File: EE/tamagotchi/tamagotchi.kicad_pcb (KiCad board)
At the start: 2 copper layers, 6.2 x 1.8 mm, 42 parts, among them J7 TAG_CONNECT, P1 USB_C_Plug_USB2.0, SW2 TL1260BQRBLK, U2 STM32G031G8Ux

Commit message: Basic Placement Complete
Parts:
- removed D2: LED, LED_SMD:LED_0603_1608Metric_Pad1.05x0.95mm_HandSolder
- removed R1: R, Resistor_SMD:R_0402_1005Metric_Pad0.72x0.64mm_HandSolder
- added BATTERY: Conn_01x02_Male, Connector_JST:JST_PH_B2B-PH-K_1x02_P2.00mm_Vertical, F.Cu at (167.5, 107.3)
- added D3: LED_BRGY, Library:EAST1616RGYA0_EVE, F.Cu at (169.2, 87.2)
- added D4: LED_BRGY, Library:EAST1616RGYA0_EVE, F.Cu at (152.7, 72.6)
- added D5: LED_BRGY, Library:EAST1616RGYA0_EVE, F.Cu at (137.5, 87.2)
- added J3: Conn_01x07, Library:MOLEX_532610771, B.Cu at (152.0, 79.5)
- added JP2: SolderJumper_2_Bridged, Jumper:SolderJumper-2_P1.3mm_Bridged2Bar_RoundedPad1.0x1.5mm, F.Cu at (165.5, 100.9)
- added JP3: SolderJumper_2_Bridged, Jumper:SolderJumper-2_P1.3mm_Bridged2Bar_RoundedPad1.0x1.5mm, F.Cu at (156.0, 100.1)
- added JP4: SolderJumper_2_Bridged, Jumper:SolderJumper-2_P1.3mm_Bridged2Bar_RoundedPad1.0x1.5mm, B.Cu at (160.8, 102.5)
- added L1: ~, Library:UT Transformer, F.Cu at (161.5, 105.8)
- added Q1: Q_NMOS_GSD, Package_TO_SOT_SMD:SOT-23, B.Cu at (155.5, 87.9)
- added Q2: Q_NMOS_GSD, Package_TO_SOT_SMD:SOT-23, F.Cu at (166.2, 78.8)
- added Q3: Q_NMOS_GSD, Package_TO_SOT_SMD:SOT-23, F.Cu at (141.9, 78.2)
- added Q4: Q_NMOS_GSD, Package_TO_SOT_SMD:SOT-23, F.Cu at (161.8, 98.0)
- added Q5: Q_PMOS_GSD, Package_TO_SOT_SMD:SOT-23, F.Cu at (162.4, 91.8)
- added Q7: Q_NMOS_GSD, Package_TO_SOT_SMD:SOT-23, F.Cu at (165.7, 84.3)
- added UT: Conn_01x02_Male, Connector_JST:JST_PH_B2B-PH-K_1x02_P2.00mm_Vertical, F.Cu at (157.0, 107.2)
- C1, D1, D6, D7, D8, D9, J7, R14, R15, R16, R17, R2, R27, R28, R3, R4: moved to B.Cu
- moved R29 81.1 mm to (141.2, 86.3), turned to 90 degrees
- moved C5 78.6 mm to (151.8, 92.2), turned to -90 degrees
- moved R28 78.3 mm to (164.2, 76.4), turned to -90 degrees
- moved R27 75.8 mm to (165.8, 76.4), turned to -90 degrees
- moved R13 75.5 mm to (137.2, 90.1), turned to 90 degrees
- moved R10 73.7 mm to (149.9, 72.0)
- moved J7 54.9 mm to (144.5, 96.5)
- moved R9 53.5 mm to (163.0, 77.8), turned to 0 degrees
- moved R8 51.0 mm to (162.4, 79.4), turned to -90 degrees
- moved R7 49.5 mm to (169.8, 84.2), turned to -90 degrees
- moved R12 46.1 mm to (138.8, 77.2)
- moved R11 43.8 mm to (138.2, 79.1), turned to -90 degrees
- moved C1 43.6 mm to (147.2, 84.5), turned to -90 degrees
- moved R5 42.4 mm to (161.9, 84.6), turned to -90 degrees
- moved R4 42.0 mm to (158.7, 86.9)
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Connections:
- JP1 pad 1: /Power/VBAT_BRIDGED -> Net-(J8-Pin_1)
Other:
- board size 6.2 x 1.8 mm -> 34.8 x 38.8 mm

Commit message: Migrated to 4 Layer. Added 3v3 and gnd layers
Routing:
- added copper zone on In2.Cu, net +3V3
- added copper zone on In1.Cu, net GND
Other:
- copper layers 2 -> 4
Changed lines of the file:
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@@
 	(layers
 		(0 "F.Cu" signal)
+		(4 "In1.Cu" signal)
+		(6 "In2.Cu" signal)
 		(2 "B.Cu" signal)
 		(9 "F.Adhes" user "F.Adhesive")
@@
 	)
 	(setup
+		(stackup
+			(layer "F.SilkS"
+				(type "Top Silk Screen")
+			)
+			(layer "F.Paste"
+				(type "Top Solder Paste")
+			)
+			(layer "F.Mask"
+				(type "Top Solder Mask")
+				(thickness 0.01)
+			)
+			(layer "F.Cu"
+				(type "copper")
+				(thickness 0.035)
+			)
+			(layer "dielectric 1"
+				(type "prepreg")
+				(thickness 0.1)
+				(material "FR4")
+				(epsilon_r 4.5)
+				(loss_tangent 0.02)
+			)
+			(layer "In1.Cu"
+				(type "copper")
+				(thickness 0.035)
+			)
+			(layer "dielectric 2"
+				(type "core")
+				(thickness 1.24)
+				(material "FR4")
+				(epsilon_r 4.5)
+				(loss_tangent 0.02)
+			)
+			(layer "In2.Cu"
+				(type "copper")
+				(thickness 0.035)
+			)
+			(layer "dielectric 3"
+				(type "prepreg")
+				(thickness 0.1)
+				(material "FR4")
+				(epsilon_r 4.5)
+				(loss_tangent 0.02)
+			)
+			(layer "B.Cu"
+				(type "copper")
+				(thickness 0.035)
+			)
+			(layer "B.Mask"
+				(type "Bottom Solder Mask")
+				(thickness 0.01)
+			)
+			(layer "B.Paste"
+				(type "Bottom Solder Paste")
+			)
+			(layer "B.SilkS"
+				(type "Bottom Silk Screen")
+			)
+			(copper_finish "None")
+			(dielectric_constraints no)
+		)
 		(pad_to_mask_clearance 0)
 		(allow_soldermask_bridges_in_footprints no)
@@
 		(layer "Edge.Cuts")
 	)
+	(zone
+		(net 2)
+		(net_name "GND")
+		(layer "In1.Cu")
+		(hatch edge 0.5)
+		(connect_pads
+			(clearance 0.5)
+		)
+		(min_thickness 0.25)
+		(filled_areas_thickness no)
+		(fill yes
+			(thermal_gap 0.5)
+			(thermal_bridge_width 0.5)
+		)
+		(polygon
+			(pts
+				(xy 136 71) (xy 170.75 71) (xy 170.75 109.75) (xy 136 109.75)
+			)
+		)
+	)
+	(zone
+		(net 1)
+		(net_name "+3V3")
+		(layer "In2.Cu")
+		(hatch edge 0.5)
+		(priority 1)
+		(connect_pads
+			(clearance 0.5)
+		)
+		(min_thickness 0.25)
+		(filled_areas_thickness no)
+		(fill yes
+			(thermal_gap 0.5)
+			(thermal_bridge_width 0.5)
+		)
+		(polygon
+			(pts
+				(xy 136 71) (xy 170.75 71) (xy 170.75 109.75) (xy 136 109.75)
+			)
+		)
+	)
 	(embedded_fonts no)

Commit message: Minor Placement update
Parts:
- JP1, Q1, R3, R4: moved to F.Cu
- JP3: moved to B.Cu
- moved Q2 21.0 mm to (145.3, 76.8), turned to 90 degrees
- moved D1 19.7 mm to (153.4, 91.8)
- moved R2 19.7 mm to (156.2, 91.8)
- moved R9 18.9 mm to (144.3, 80.0), turned to 90 degrees
- moved Q7 18.2 mm to (151.8, 96.0), turned to -90 degrees
- moved R8 16.5 mm to (146.0, 80.6), turned to 0 degrees
- moved R6 13.5 mm to (153.0, 92.7), turned to -90 degrees
- moved D7 13.2 mm to (153.4, 72.2)
- moved R15 13.1 mm to (156.2, 72.2)
- moved R5 13.0 mm to (151.4, 92.2), turned to 180 degrees
- moved R11 12.8 mm to (150.9, 80.6), turned to 0 degrees
- moved Q1 11.1 mm to (155.2, 76.8), turned to 90 degrees
- moved R12 10.7 mm to (149.1, 80.0), turned to 90 degrees
- moved UT 10.4 mm to (167.4, 107.2)
- moved BATTERY 9.41 mm to (158.3, 105.2), turned to -90 degrees
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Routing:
- net VBUS: track 0.00 -> 13.3 mm

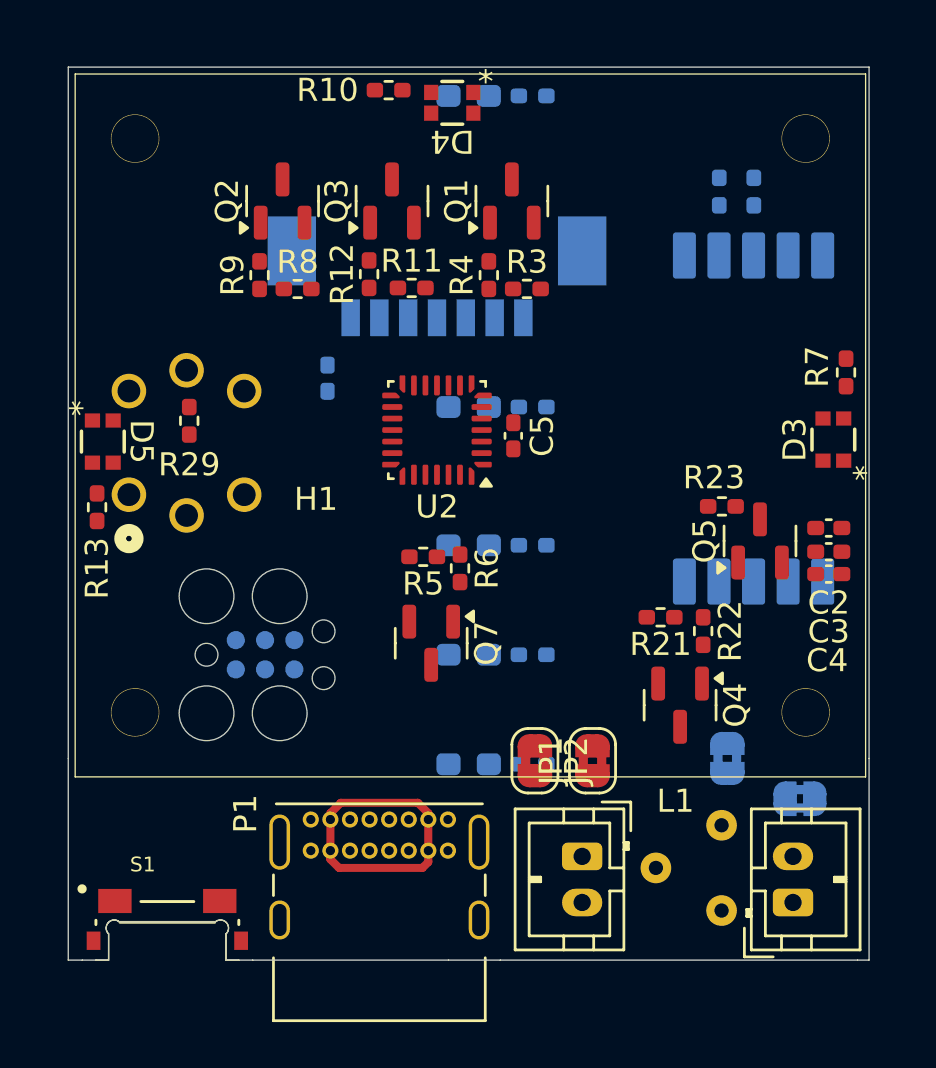
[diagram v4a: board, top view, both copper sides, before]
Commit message: Removed LEDs
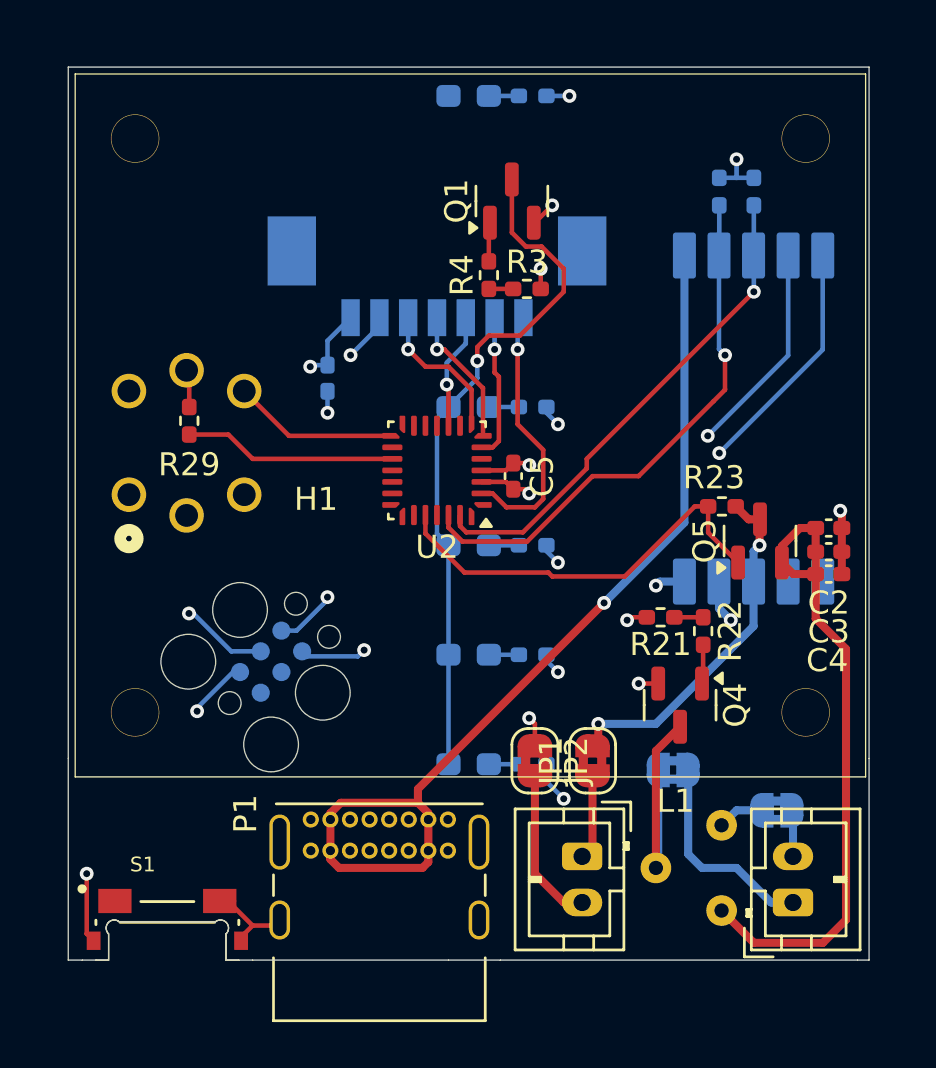
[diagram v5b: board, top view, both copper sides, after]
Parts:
- removed D3, D4, D5: LED_BRGY, Library:EAST1616RGYA0_EVE
- removed Q2, Q3, Q7: Q_NMOS_GSD, Package_TO_SOT_SMD:SOT-23
- removed R10, R13, R7: R, Resistor_SMD:R_0402_1005Metric_Pad0.72x0.64mm_HandSolder
- removed R11, R5, R8: 100k, Resistor_SMD:R_0402_1005Metric_Pad0.72x0.64mm_HandSolder
- removed R12, R6, R9: 33, Resistor_SMD:R_0402_1005Metric_Pad0.72x0.64mm_HandSolder
- moved JP3 2.40 mm to (162.2, 101.5), turned to 180 degrees
- moved C5 1.75 mm to (155.3, 88.8)
- moved U2 1.75 mm to (152.0, 88.5)
- moved JP4 1.12 mm to (166.8, 103.2)
- moved J7 0.40 mm to (144.8, 96.8), turned to 45 degrees
- renumbered UT to J1, BATTERY to J8
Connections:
- J3 pad 3: /Display/MOSI{SPI} -> /Display/MOSI
- J3 pad 4: /Display/CLK{SPI} -> /Display/CLK
- J3 pad 5: /Display/CS{SPI} -> /Display/CS
- J3 pad 6: /Display/DC{SPI} -> /Display/DC
- J3 pad 7: /Display/RST{SPI} -> /Display/RST
- J7 pad 5: /MCU/SWDCLK -> /MCU/SWCLK
- R29 pad 1: /Vape/VAPE_LED -> /MCU/VAPE_LED
- U2 pad 10: /MCU/CS{SPI} -> /Display/CS
- U2 pad 11: /MCU/DC{SPI} -> unconnected-(U2-PA5-Pad11)
- U2 pad 12: /MCU/RST{SPI} -> unconnected-(U2-PA6-Pad12)
- U2 pad 14: /Display/GREEN_EN -> unconnected-(U2-PB0-Pad14)
- U2 pad 15: /Display/YELLOW_EN -> /MCU/VAPE_SW
- U2 pad 17: unconnected-(U2-PC6-Pad17) -> /MCU/VAPE_LED
- U2 pad 2: unconnected-(U2-PC15-Pad2) -> /Display/RST
- U2 pad 22: /MCU/VAPE_SW -> unconnected-(U2-PA15-Pad22)
- U2 pad 23: /Display/RED_EN -> unconnected-(U2-PB3-Pad23)
- U2 pad 6: unconnected-(U2-PA0-Pad6) -> /Display/DC
- U2 pad 7: /MCU/CLK{SPI} -> /Display/CLK
- U2 pad 8: /MCU/MOSI{SPI} -> /Display/MOSI
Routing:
- net Net-(D1-K): track 0.00 -> 30.0 mm, vias 0 -> 1
- net VBUS: track 13.3 -> 41.8 mm, vias 0 -> 1
- net /Vape/VBAT_CONT: track 0.00 -> 28.1 mm
- net GND: track 0.00 -> 25.9 mm, vias 0 -> 12
- net /MCU/SCL: track 0.00 -> 23.6 mm, vias 0 -> 1
- net /MCU/SDA: track 0.00 -> 21.7 mm, vias 0 -> 1
- net /MCU/VAPE_EN_N: track 0.00 -> 18.1 mm
- net +3V3: track 0.00 -> 18.0 mm, vias 0 -> 10
- net /VBAT: track 0.00 -> 15.6 mm, vias 0 -> 2
- net /Display/RST: track 0.00 -> 11.5 mm, vias 0 -> 1
- net /Vape/UT_OUT-: track 0.00 -> 10.9 mm
- net /MCU/CE_N: track 0.00 -> 10.4 mm, vias 0 -> 1
- net /MCU/INT_N: track 0.00 -> 9.27 mm, vias 0 -> 1
- net /MCU/VAPE_LED: track 0.00 -> 9.25 mm
- net Net-(J1-Pin_1): track 0.00 -> 9.07 mm
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
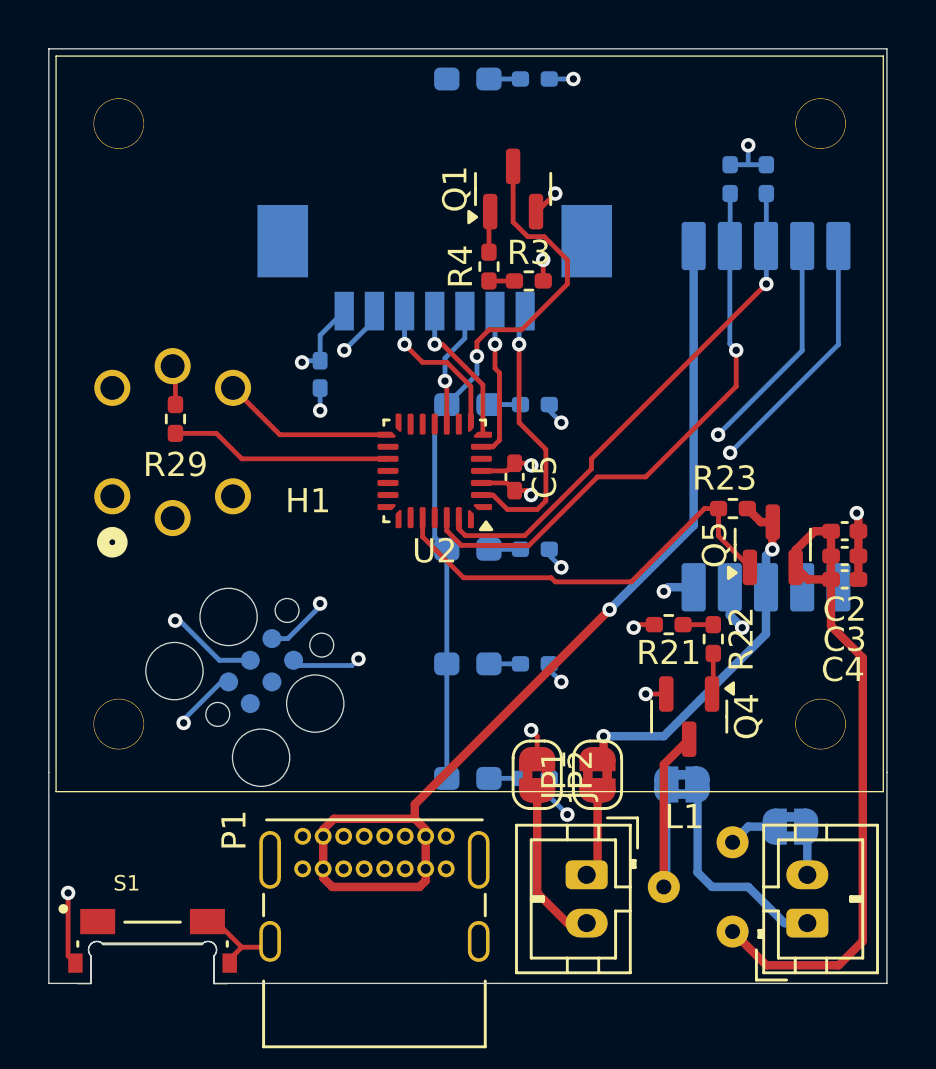
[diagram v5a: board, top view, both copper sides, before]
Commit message: First pass routing / placement & LED -> Buzzer for warning
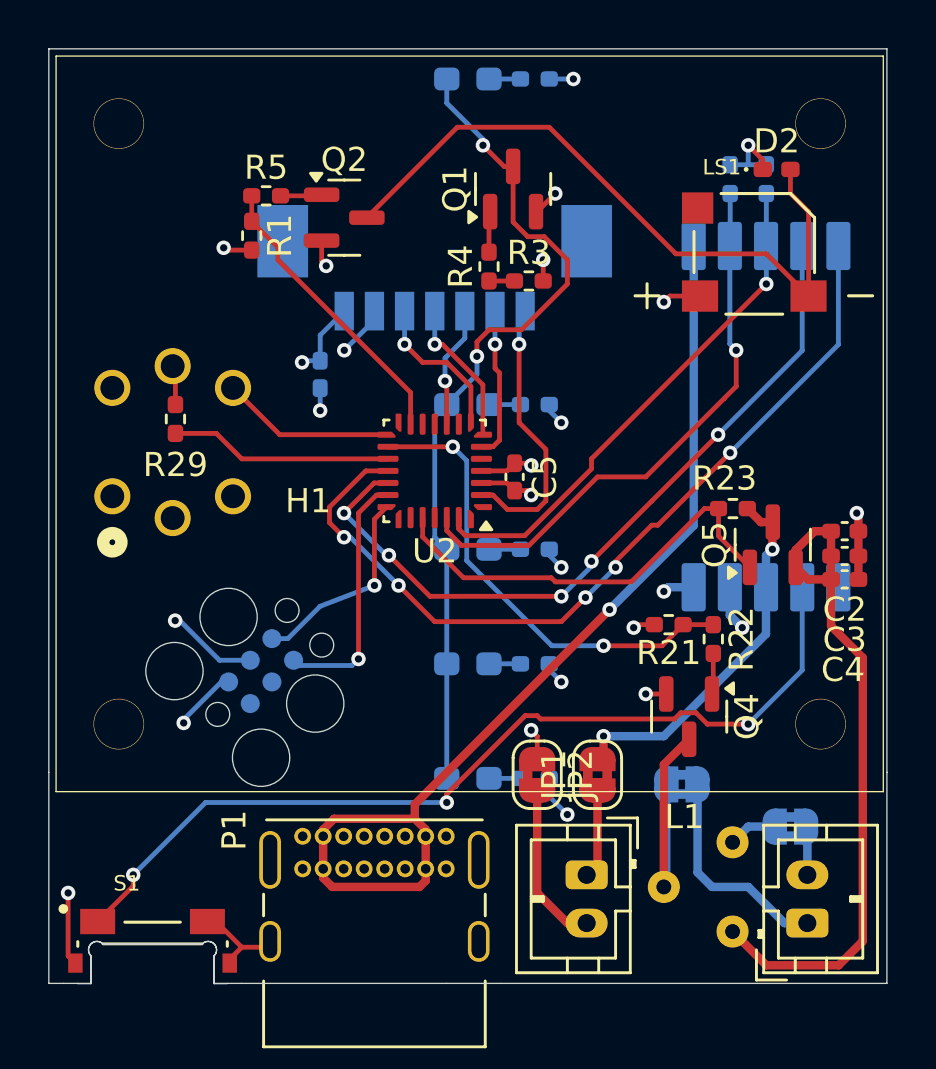
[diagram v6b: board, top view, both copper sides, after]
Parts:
- added D2: D, Diode_SMD:D_0402_1005Metric_Pad0.77x0.64mm_HandSolder, F.Cu at (166.2, 76.0)
- added LS1: SMT-0540-T-10-R, Library:XDCR_SMT-0540-T-10-R, F.Cu at (165.2, 79.5)
- added Q2: Q_NMOS_GSD, Package_TO_SOT_SMD:SOT-23, F.Cu at (148.2, 78.0)
- added R1: 100k, Resistor_SMD:R_0402_1005Metric_Pad0.72x0.64mm_HandSolder, F.Cu at (144.4, 78.7)
- added R5: 33, Resistor_SMD:R_0402_1005Metric_Pad0.72x0.64mm_HandSolder, F.Cu at (145.0, 77.1)
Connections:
- U2 pad 13: unconnected-(U2-PA7-Pad13) -> /Display/BUZZ_PWM
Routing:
- net /Power/SWITCH: track 0.00 -> 37.9 mm, vias 0 -> 3
- net Net-(D2-A): track 0.00 -> 28.3 mm
- net /MCU/CE_N: track 10.4 -> 35.5 mm, vias 1 -> 5
- net /MCU/INT_N: track 9.27 -> 31.4 mm, vias 1 -> 5
- net /MCU/VAPE_PWM: track 1.25 -> 19.7 mm, vias 0 -> 2
- net /Display/BUZZ_PWM: track 0.00 -> 12.2 mm
- net /MCU/SWDIO: track 2.89 -> 10.5 mm
- net /MCU/SWCLK: track 2.67 -> 8.42 mm
- net Net-(D1-K): track 30.0 -> 35.0 mm, vias 1 -> 2
- net +3V3: track 18.0 -> 20.9 mm, vias 10 -> 11
- net GND: track 25.9 -> 28.2 mm, vias 12 -> 14
- net Net-(Q2-G): track 0.00 -> 1.72 mm

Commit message: Silkscreen Fix
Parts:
- renumbered JP2 to BATGND, JP4 to UT+, JP3 to UT-, JP1 to VBAT
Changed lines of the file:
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@@
 		(descr "SMD Solder Jumper, 1x1.5mm, rounded Pads, 0.3mm gap, bridged with 2 copper strips")
 		(tags "net tie solder jumper bridged")
-		(property "Reference" "JP1"
-			(at 0 -1.8 90)
+		(property "Reference" "VBAT"
+			(at 3.350001 0 90)
 			(layer "F.SilkS")
 			(effects
@@
 		(descr "SMD Solder Jumper, 1x1.5mm, rounded Pads, 0.3mm gap, bridged with 2 copper strips")
 		(tags "net tie solder jumper bridged")
-		(property "Reference" "JP2"
-			(at 0 -1.8 90)
+		(property "Reference" "BATGND"
+			(at -2.100001 1.75 90)
 			(layer "F.SilkS")
 			(effects
@@
 		(at 160.2375 86.175 -90)
 		(property "Reference" "U1"
-			(at 0 1 90)
+			(at 1.575 0.7375 90)
 			(unlocked yes)
 			(layer "B.SilkS")
@@
 		(descr "SMD Solder Jumper, 1x1.5mm, rounded Pads, 0.3mm gap, bridged with 2 copper strips")
 		(tags "net tie solder jumper bridged")
-		(property "Reference" "JP4"
+		(property "Reference" "UT+"
 			(at 0 1.8 0)
 			(layer "B.SilkS")
@@
 		(descr "SMD Solder Jumper, 1x1.5mm, rounded Pads, 0.3mm gap, bridged with 2 copper strips")
 		(tags "net tie solder jumper bridged")
-		(property "Reference" "JP3"
+		(property "Reference" "UT-"
 			(at 0 1.8 0)
 			(layer "B.SilkS")
